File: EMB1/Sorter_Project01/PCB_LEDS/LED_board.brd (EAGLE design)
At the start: 100 x 80 mm, 10 parts

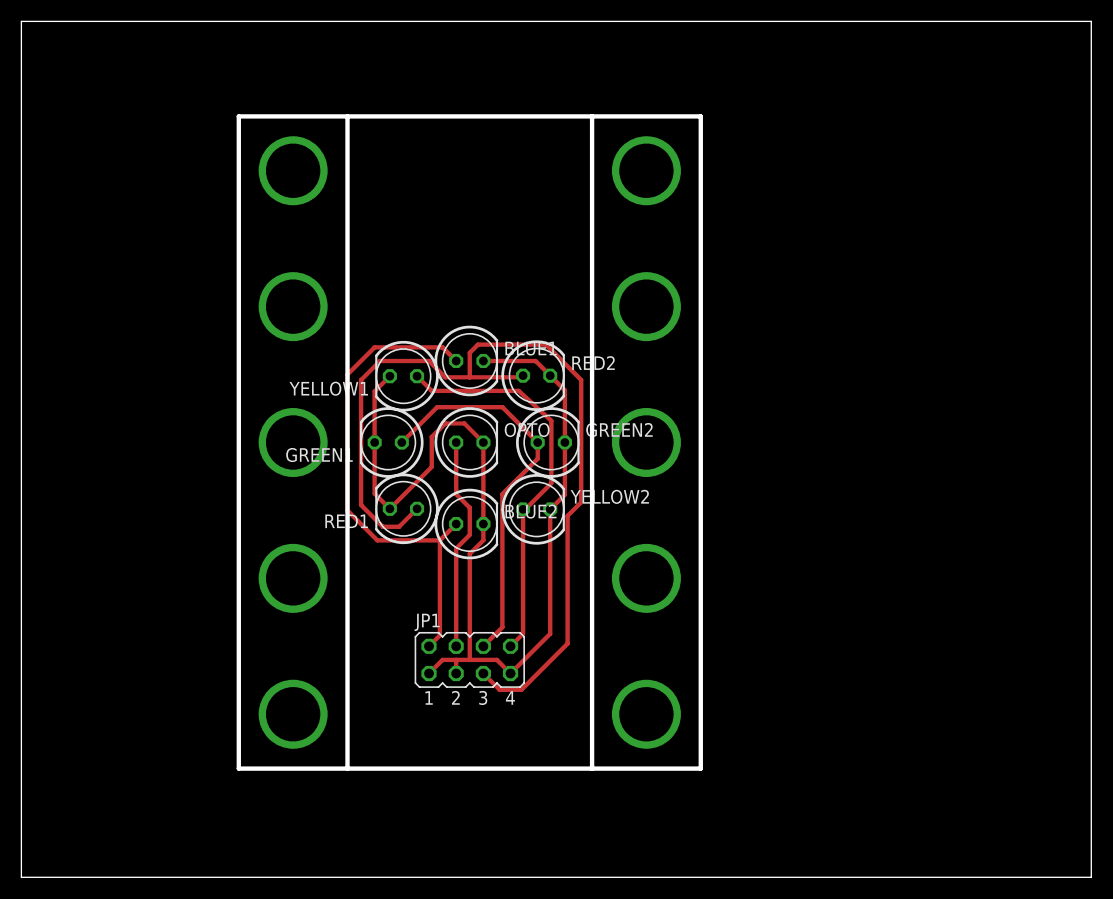
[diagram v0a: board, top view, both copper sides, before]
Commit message: new board design for leds with 2x3 connector
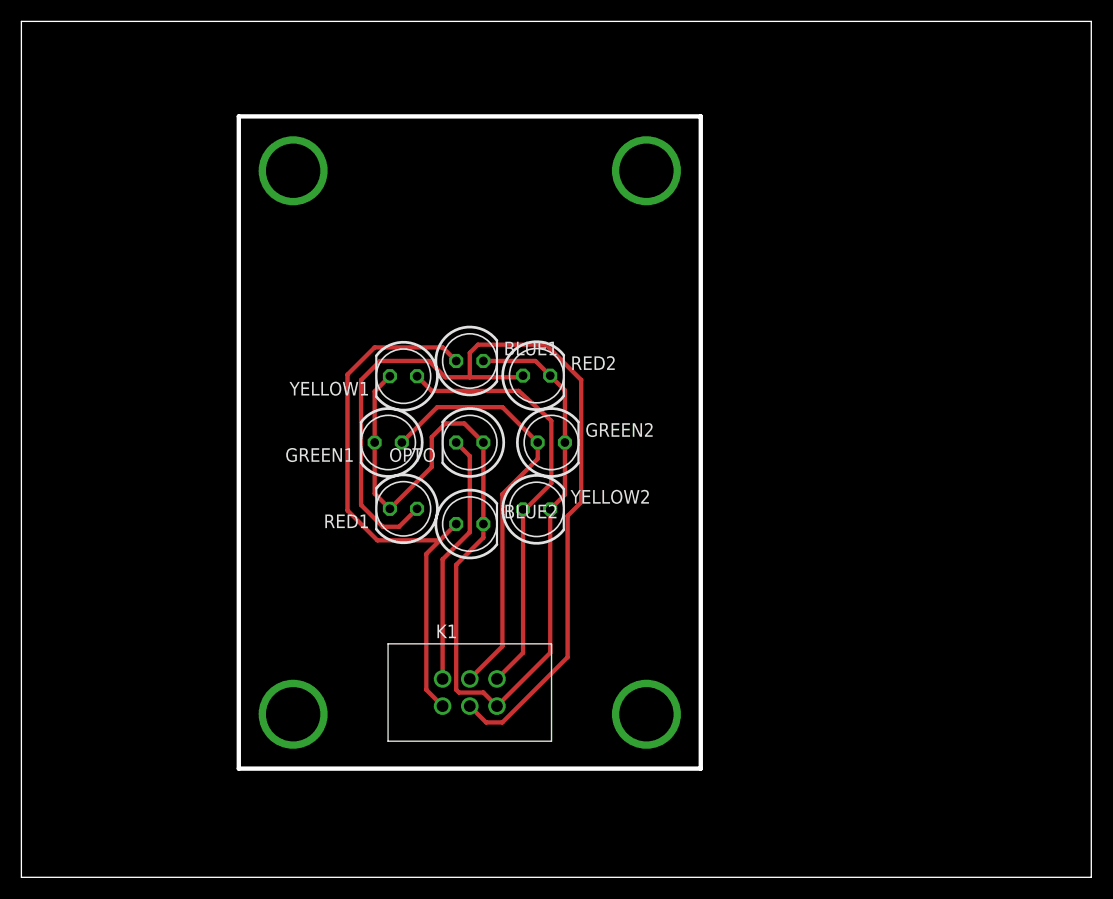
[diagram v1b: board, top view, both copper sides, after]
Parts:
- removed JP1: (no value), jumper:JP4Q
- added K1: 61200621621, Wurth_Elektronik_Electromechanic_Wire_to_Board_Connectors_rev15c:61200621621
- turned OPTO to 180 degrees
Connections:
- net GND: now also K1.5, OPTO.A; no longer JP1.1, JP1.3, JP1.7, OPTO.K
- net N$1: now also K1.3; no longer JP1.5
- net N$2: now also K1.4; no longer JP1.6
- net N$3: now also K1.1; no longer JP1.2
- net N$4: now also K1.6; no longer JP1.8
- net N$5: now also K1.2, OPTO.K; no longer JP1.4, OPTO.A
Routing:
- net N$3: track 46.7 -> 53.0 mm
- net N$2: track 36.6 -> 40.2 mm
- net N$5: track 20.1 -> 23.7 mm
- net N$4: track 37.0 -> 40.6 mm
- net N$1: track 85.0 -> 88.3 mm
- net GND: track 96.1 -> 97.5 mm
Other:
- outline, holes or cut-outs redrawn
